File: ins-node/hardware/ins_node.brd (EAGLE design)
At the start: 54.7 x 43.2 mm, 15 parts, among them Q1 MOSFET-2N7000, Q2 MOSFET-2N7000, U1 TINY85-20-DIP

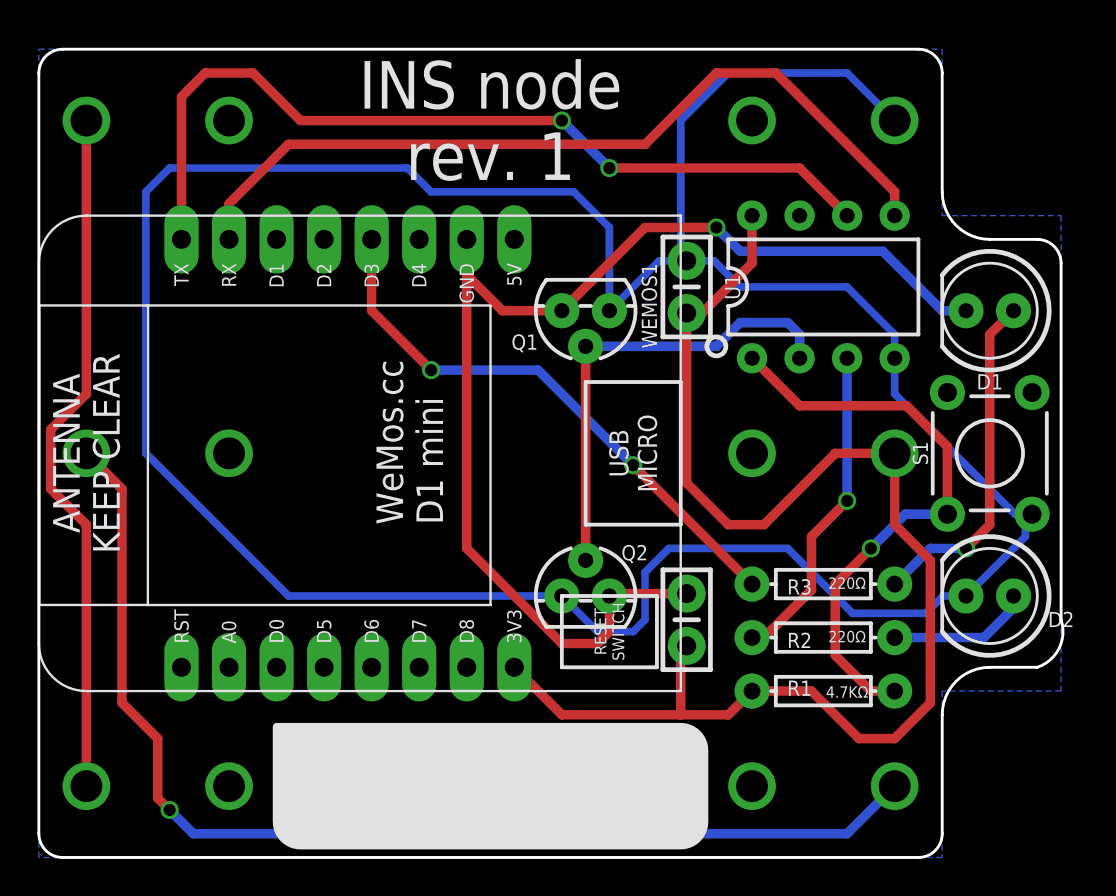
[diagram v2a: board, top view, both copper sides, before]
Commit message: Update battery position and orientation for consistency
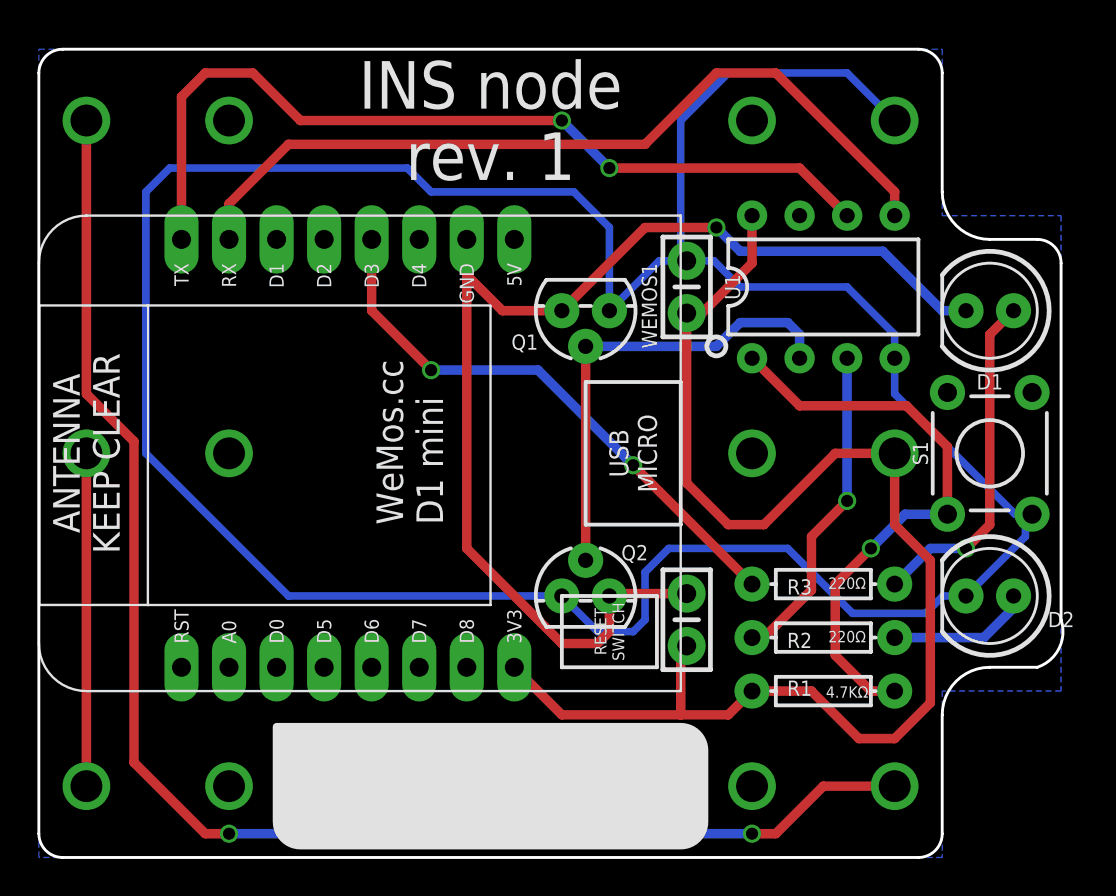
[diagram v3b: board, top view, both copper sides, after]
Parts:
- turned BT2 to 180 degrees
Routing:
- net N$5: track 61.2 -> 17.8 mm, vias 1 -> 0
- net N$1: track 37.1 -> 78.6 mm, vias 0 -> 2
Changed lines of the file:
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@@
 <attribute name="VALUE" x="50.8" y="46.355" size="0.4064" layer="27" ratio="10" rot="R270"/>
 </element>
-<element name="BT2" library="SparkFun-Batteries" library_urn="urn:adsk.eagle:library:508" package="BATTERY-AAA" package3d_urn="urn:adsk.eagle:package:37212/1" value="" x="49.53" y="34.29" smashed="yes" rot="MR0">
-<attribute name="NAME" x="30.099" y="34.29" size="0.8128" layer="26" font="vector" ratio="20" rot="MR90" align="bottom-center"/>
-<attribute name="PROD_ID" value="BATT-08571" x="49.53" y="34.29" size="1.778" layer="28" rot="MR0" display="off"/>
-<attribute name="SF_SKU" value="PRT-12718" x="49.53" y="34.29" size="1.778" layer="28" rot="MR0" display="off"/>
-<attribute name="VALUE" x="68.58" y="34.29" size="0.6096" layer="28" font="vector" ratio="20" rot="MR90" align="top-center"/>
+<element name="BT2" library="SparkFun-Batteries" library_urn="urn:adsk.eagle:library:508" package="BATTERY-AAA" package3d_urn="urn:adsk.eagle:package:37212/1" value="" x="49.53" y="34.29" smashed="yes" rot="MR180">
+<attribute name="NAME" x="30.861" y="34.29" size="0.8128" layer="26" font="vector" ratio="20" rot="MR270" align="bottom-center"/>
+<attribute name="PROD_ID" value="BATT-08571" x="49.53" y="34.29" size="1.778" layer="28" rot="MR180" display="off"/>
+<attribute name="SF_SKU" value="PRT-12718" x="49.53" y="34.29" size="1.778" layer="28" rot="MR180" display="off"/>
+<attribute name="VALUE" x="30.48" y="34.29" size="0.6096" layer="28" font="vector" ratio="20" rot="MR270" align="top-center"/>
 </element>
 <element name="BT1" library="SparkFun-Batteries" library_urn="urn:adsk.eagle:library:508" package="BATTERY-AAA" package3d_urn="urn:adsk.eagle:package:37212/1" value="" x="49.53" y="69.85" smashed="yes" rot="MR180">
@@
 <attribute name="PROD_ID" value="CAP-08370" x="60.0075" y="60.96" size="1.27" layer="27" ratio="15" rot="R90" display="off"/>
 </element>
-<element name="BT3" library="SparkFun-Batteries" library_urn="urn:adsk.eagle:library:508" package="BATTERY-AAA" package3d_urn="urn:adsk.eagle:package:37212/1" value="" x="49.53" y="52.07" rot="MR0">
+<element name="BT3" library="SparkFun-Batteries" library_urn="urn:adsk.eagle:library:508" package="BATTERY-AAA" package3d_urn="urn:adsk.eagle:package:37212/1" value="" x="49.53" y="52.07" smashed="yes" rot="MR0">
+<attribute name="NAME" x="30.099" y="52.07" size="0.8128" layer="26" font="vector" ratio="20" rot="MR90" align="bottom-center"/>
 <attribute name="PROD_ID" value="BATT-08571" x="49.53" y="52.07" size="1.778" layer="28" rot="MR0" display="off"/>
 <attribute name="SF_SKU" value="PRT-12718" x="49.53" y="52.07" size="1.778" layer="28" rot="MR0" display="off"/>
+<attribute name="VALUE" x="68.58" y="52.07" size="0.6096" layer="28" font="vector" ratio="20" rot="MR90" align="top-center"/>
 </element>
 <element name="Q1" library="SparkFun-DiscreteSemi" package="TO-92" value="MOSFET-2N7000" x="54.61" y="59.69" smashed="yes" rot="R180">
@@
 <contactref element="BT1" pad="PWR@1"/>
 <contactref element="BT2" pad="GND@1"/>
-<wire x1="27.94" y1="34.29" x2="27.94" y2="48.26" width="0.508" layer="1"/>
-<wire x1="27.94" y1="48.26" x2="26.035" y2="50.165" width="0.508" layer="1"/>
-<wire x1="26.035" y1="50.165" x2="26.035" y2="53.34" width="0.508" layer="1"/>
-<wire x1="26.035" y1="53.34" x2="27.94" y2="55.245" width="0.508" layer="1"/>
 <wire x1="27.94" y1="55.245" x2="27.94" y2="69.85" width="0.508" layer="1"/>
+<wire x1="71.12" y1="34.29" x2="67.31" y2="34.29" width="0.508" layer="1"/>
+<wire x1="67.31" y1="34.29" x2="64.77" y2="31.75" width="0.508" layer="1"/>
+<wire x1="64.77" y1="31.75" x2="63.5" y2="31.75" width="0.508" layer="1"/>
+<via x="63.5" y="31.75" extent="1-16" drill="0.65"/>
+<wire x1="63.5" y1="31.75" x2="35.56" y2="31.75" width="0.508" layer="16"/>
+<via x="35.56" y="31.75" extent="1-16" drill="0.65"/>
+<wire x1="35.56" y1="31.75" x2="34.29" y2="31.75" width="0.508" layer="1"/>
+<wire x1="34.29" y1="31.75" x2="30.48" y2="35.56" width="0.508" layer="1"/>
+<wire x1="30.48" y1="35.56" x2="30.48" y2="52.705" width="0.508" layer="1"/>
+<wire x1="30.48" y1="52.705" x2="27.94" y2="55.245" width="0.508" layer="1"/>
 </signal>
 <signal name="GND">
@@
 <contactref element="C1" pad="1"/>
 <contactref element="BT3" pad="PWR@1"/>
-<wire x1="71.12" y1="48.26" x2="71.12" y2="52.07" width="0.508" layer="1"/>
 <wire x1="73.025" y1="46.355" x2="71.12" y2="48.26" width="0.508" layer="1"/>
 <wire x1="53.34" y1="38.1" x2="59.69" y2="38.1" width="0.508" layer="1"/>
 <wire x1="53.34" y1="38.1" x2="50.8" y2="40.64" width="0.508" layer="1"/>
-<wire x1="71.12" y1="52.07" x2="67.945" y2="52.07" width="0.508" layer="1"/>
 <wire x1="67.945" y1="52.07" x2="64.135" y2="48.26" width="0.508" layer="1"/>
 <wire x1="64.135" y1="48.26" x2="62.23" y2="48.26" width="0.508" layer="1"/>
@@
 <wire x1="71.12" y1="36.83" x2="73.025" y2="38.735" width="0.508" layer="1"/>
 <wire x1="73.025" y1="38.735" x2="73.025" y2="46.355" width="0.508" layer="1"/>
+<wire x1="71.10336875" y1="52.07" x2="71.12" y2="52.07" width="0.508" layer="1"/>
+<wire x1="71.10336875" y1="52.07" x2="67.945" y2="52.07" width="0.508" layer="1"/>
+<wire x1="71.12" y1="48.26" x2="71.12" y2="52.05336875" width="0.508" layer="1"/>
+<wire x1="71.12" y1="52.05336875" x2="71.10336875" y2="52.07" width="0.508" layer="1"/>
 </signal>
 <signal name="TX">
@@
 <contactref element="BT2" pad="PWR@1"/>
 <contactref element="BT3" pad="GND@1"/>
-<wire x1="29.845" y1="50.165" x2="29.845" y2="38.735" width="0.508" layer="1"/>
-<wire x1="29.845" y1="50.165" x2="27.94" y2="52.07" width="0.508" layer="1"/>
-<wire x1="29.845" y1="38.735" x2="31.75" y2="36.83" width="0.508" layer="1"/>
-<wire x1="31.75" y1="36.83" x2="31.75" y2="33.655" width="0.508" layer="1"/>
-<wire x1="31.75" y1="33.655" x2="32.385" y2="33.02" width="0.508" layer="1"/>
-<via x="32.385" y="33.02" extent="1-16" drill="0.65"/>
-<wire x1="32.385" y1="33.02" x2="33.655" y2="31.75" width="0.508" layer="16"/>
-<wire x1="33.655" y1="31.75" x2="68.58" y2="31.75" width="0.508" layer="16"/>
-<wire x1="68.58" y1="31.75" x2="71.12" y2="34.29" width="0.508" layer="16"/>
+<wire x1="27.94" y1="34.29" x2="27.94" y2="52.07" width="0.508" layer="1"/>
 </signal>
 <signal name="N$6">

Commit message: Add pulldown resistor for MOSFETs base
Add a pulldown resistor for the MOSFET trigger pins so to make sure
that we have a clean signal that only activates the Wifi module
when we want.

This change constitutes HW Rev. 2
Fixes #71
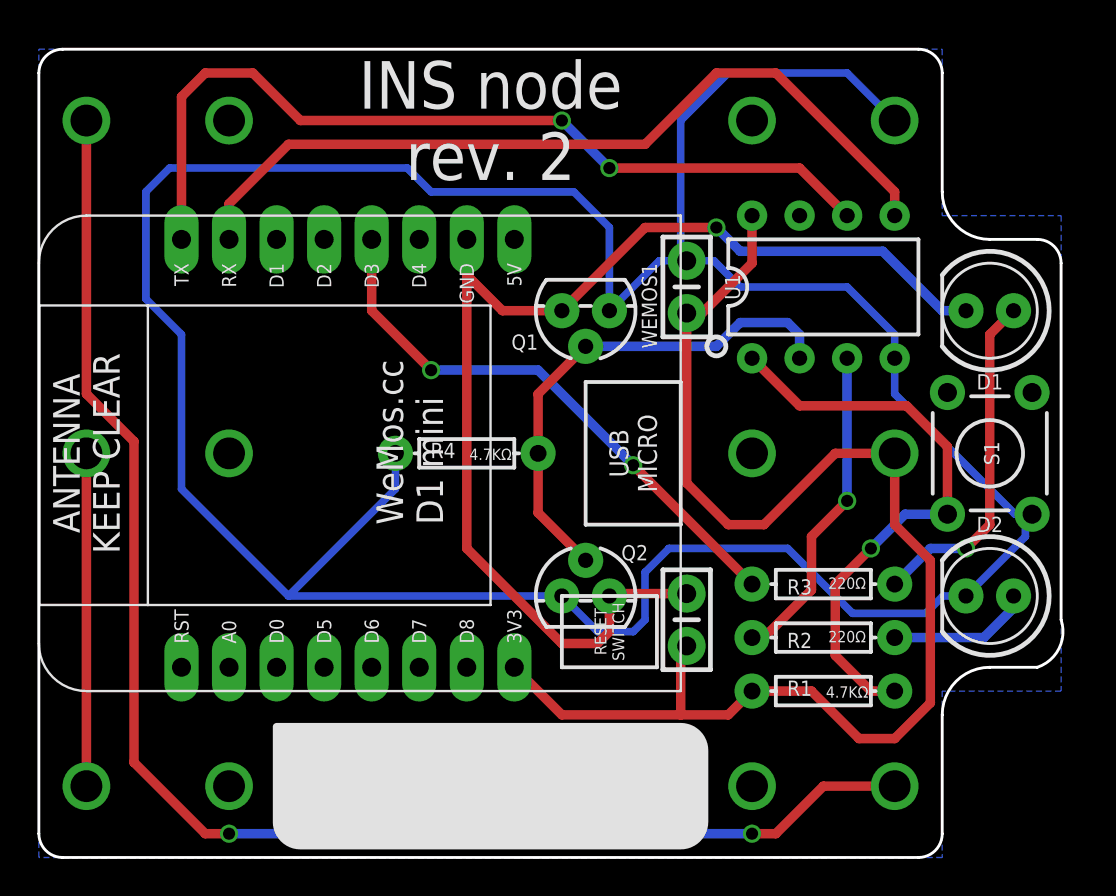
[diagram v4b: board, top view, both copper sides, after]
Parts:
- added R4: 4.7KΩ, SparkFun-Resistors:AXIAL-0.3
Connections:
- net GND: now also R4.P$1
- net WEMOS_ON: now also R4.P$2
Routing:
- net GND: track 157.0 -> 166.9 mm
- net WEMOS_ON: track 24.9 -> 27.0 mm
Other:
- board text added: "INS node rev. 2"
- board text removed: "INS node rev. 1"
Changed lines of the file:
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@@
 <?xml version="1.0" encoding="utf-8"?>
 <!DOCTYPE eagle SYSTEM "eagle.dtd">
-<eagle version="8.3.0">
+<eagle version="8.4.3">
 <drawing>
 <settings>
@@
 <wire x1="78.74" y1="63.5" x2="80.01" y2="62.23" width="0.1524" layer="20" curve="-90"/>
 <text x="49.53" y="69.85" size="2.54" layer="21" font="vector" ratio="15" align="center">INS node
-rev. 1</text>
+rev. 2</text>
 <polygon width="0.4064" layer="21">
 <vertex x="38.1" y="37.465"/>
@@
 <param name="dpMaxLengthDifference" value="10mm"/>
 <param name="dpGapFactor" value="2.5"/>
-<param name="checkGrid" value="0"/>
 <param name="checkAngle" value="0"/>
 <param name="checkFont" value="1"/>
 <param name="checkRestrict" value="0"/>
+<param name="checkStop" value="0"/>
 <param name="useDiameter" value="13"/>
 <param name="maxErrors" value="50"/>
@@
 </element>
 <element name="S1" library="SparkFun-Switches" library_urn="urn:adsk.eagle:library:535" package="TACTILE_SWITCH_PTH_6.0MM" package3d_urn="urn:adsk.eagle:package:40163/1" value="MOMENTARY-SWITCH-SPST-PTH-6.0MM" x="76.2" y="52.07" smashed="yes" rot="R90">
-<attribute name="NAME" x="72.898" y="52.07" size="0.8128" layer="25" font="vector" ratio="20" rot="R90" align="bottom-center"/>
+<attribute name="NAME" x="76.708" y="52.07" size="0.8128" layer="25" font="vector" ratio="20" rot="R90" align="bottom-center"/>
 <attribute name="PROD_ID" value=" SWCH-08441" x="76.2" y="52.07" size="1.778" layer="27" rot="R90" display="off"/>
 <attribute name="SF_SKU" value="COM-00097" x="76.2" y="52.07" size="1.778" layer="27" rot="R90" display="off"/>
@@
 </element>
 <element name="D2" library="SparkFun-LED" library_urn="urn:adsk.eagle:library:529" package="LED_5MM-KIT" package3d_urn="urn:adsk.eagle:package:39357/1" value="" x="76.2" y="44.45" smashed="yes" rot="R180">
-<attribute name="NAME" x="80.01" y="43.5991" size="0.8128" layer="25" font="vector" ratio="20" rot="R180" align="bottom-center"/>
+<attribute name="NAME" x="76.2" y="48.6791" size="0.8128" layer="25" font="vector" ratio="20" rot="R180" align="bottom-center"/>
 <attribute name="VALUE" x="76.1746" y="47.8409" size="0.6096" layer="27" font="vector" ratio="20" rot="R180" align="top-center"/>
 </element>
@@
 <element name="C2" library="SparkFun-Capacitors" library_urn="urn:adsk.eagle:library:510" package="CAP-PTH-SMALL-KIT" package3d_urn="urn:adsk.eagle:package:37428/1" value="0.1uF" x="60.0075" y="43.18" rot="R90">
 <attribute name="PROD_ID" value="CAP-08370" x="60.0075" y="43.18" size="1.778" layer="27" rot="R90" display="off"/>
+</element>
+<element name="R4" library="SparkFun-Resistors" library_urn="urn:adsk.eagle:library:532" package="AXIAL-0.3" package3d_urn="urn:adsk.eagle:package:39658/1" value="4.7KΩ" x="48.26" y="52.07" smashed="yes">
+<attribute name="NAME" x="46.99" y="51.816" size="0.8128" layer="25" font="vector" ratio="20" align="bottom-center"/>
+<attribute name="PROD_ID" value=" " x="48.26" y="52.07" size="1.778" layer="27" display="off"/>
+<attribute name="VALUE" x="49.53" y="52.324" size="0.6096" layer="25" font="vector" ratio="20" align="top-center"/>
 </element>
 </elements>
@@
 <wire x1="60.1345" y1="62.23" x2="60.0075" y2="62.357" width="0.4064" layer="16"/>
 <wire x1="53.34" y1="44.45" x2="38.735" y2="44.45" width="0.4064" layer="16"/>
-<wire x1="38.735" y1="44.45" x2="31.115" y2="52.07" width="0.4064" layer="16"/>
-<wire x1="31.115" y1="52.07" x2="31.115" y2="66.04" width="0.4064" layer="16"/>
+<wire x1="31.115" y1="60.325" x2="31.115" y2="66.04" width="0.4064" layer="16"/>
 <wire x1="31.115" y1="66.04" x2="32.385" y2="67.31" width="0.4064" layer="16"/>
 <wire x1="32.385" y1="67.31" x2="45.085" y2="67.31" width="0.4064" layer="16"/>
@@
 <vertex x="25.4" y="30.48"/>
 </polygon>
+<contactref element="R4" pad="P$1"/>
+<wire x1="38.735" y1="44.45" x2="44.45" y2="50.165" width="0.4064" layer="16"/>
+<wire x1="44.45" y1="50.165" x2="44.45" y2="52.07" width="0.4064" layer="16"/>
+<wire x1="38.735" y1="44.45" x2="33.02" y2="50.165" width="0.4064" layer="16"/>
+<wire x1="33.02" y1="50.165" x2="33.02" y2="58.42" width="0.4064" layer="16"/>
+<wire x1="33.02" y1="58.42" x2="31.115" y2="60.325" width="0.4064" layer="16"/>
 </signal>
 <signal name="VCC">
@@
 <contactref element="Q2" pad="2"/>
 <contactref element="Q1" pad="2"/>
-<wire x1="54.61" y1="46.355" x2="54.61" y2="57.785" width="0.508" layer="1"/>
 <wire x1="54.61" y1="57.785" x2="61.595" y2="57.785" width="0.508" layer="16"/>
 <wire x1="61.595" y1="57.785" x2="62.865" y2="59.055" width="0.508" layer="16"/>
@@
 <wire x1="65.405" y1="59.055" x2="66.04" y2="58.42" width="0.508" layer="16"/>
 <wire x1="66.04" y1="58.42" x2="66.04" y2="57.15" width="0.508" layer="16"/>
+<contactref element="R4" pad="P$2"/>
+<wire x1="54.61" y1="57.785" x2="52.07" y2="55.245" width="0.508" layer="1"/>
+<wire x1="52.07" y1="55.245" x2="52.07" y2="52.07" width="0.508" layer="1"/>
+<wire x1="52.07" y1="52.07" x2="52.07" y2="48.895" width="0.508" layer="1"/>
+<wire x1="52.07" y1="48.895" x2="54.61" y2="46.355" width="0.508" layer="1"/>
 </signal>
 <signal name="ATTINY_LED">
